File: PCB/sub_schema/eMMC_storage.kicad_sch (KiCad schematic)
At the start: 26 parts, among them U10 MTFC32GAZAQHD-WT, U8 MTFC32GAZAQHD-WT

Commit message: worked on BOM
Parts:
- C29, C30, C31, C32, C35, C36, C37, C38, C39, C40, C42, C43, C44, C45, C46, C48, C49, C50, C51, C52: footprint (none) -> Capacitor_SMD:C_0201_0603Metric
- C33, C34, C41, C47: footprint (none) -> Capacitor_SMD:C_0402_1005Metric
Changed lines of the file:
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@@
 			)
 		)
-		(property "Footprint" ""
+		(property "Footprint" "Capacitor_SMD:C_0201_0603Metric"
 			(at 88.9 27.94 0)
 			(effects
@@
 			)
 		)
-		(property "Footprint" ""
+		(property "Footprint" "Capacitor_SMD:C_0201_0603Metric"
 			(at 124.46 27.94 0)
 			(effects
@@
 			)
 		)
-		(property "Footprint" ""
+		(property "Footprint" "Capacitor_SMD:C_0201_0603Metric"
 			(at 31.75 128.27 0)
 			(effects
@@
 			)
 		)
-		(property "Footprint" ""
+		(property "Footprint" "Capacitor_SMD:C_0201_0603Metric"
 			(at 36.83 29.21 0)
 			(effects
@@
 			)
 		)
-		(property "Footprint" ""
+		(property "Footprint" "Capacitor_SMD:C_0201_0603Metric"
 			(at 54.61 29.21 0)
 			(effects
@@
 			)
 		)
-		(property "Footprint" ""
+		(property "Footprint" "Capacitor_SMD:C_0201_0603Metric"
 			(at 106.68 27.94 0)
 			(effects
@@
 			)
 		)
-		(property "Footprint" ""
+		(property "Footprint" "Capacitor_SMD:C_0201_0603Metric"
 			(at 270.51 29.21 0)
 			(effects
@@
 			)
 		)
-		(property "Footprint" ""
+		(property "Footprint" "Capacitor_SMD:C_0201_0603Metric"
 			(at 261.62 29.21 0)
 			(effects
@@
 			)
 		)
-		(property "Footprint" ""
+		(property "Footprint" "Capacitor_SMD:C_0201_0603Metric"
 			(at 97.79 27.94 0)
 			(effects
@@
 			)
 		)
-		(property "Footprint" ""
+		(property "Footprint" "Capacitor_SMD:C_0201_0603Metric"
 			(at 252.73 29.21 0)
 			(effects
@@
 			)
 		)
-		(property "Footprint" ""
+		(property "Footprint" "Capacitor_SMD:C_0201_0603Metric"
 			(at 182.88 30.48 0)
 			(effects
@@
 			)
 		)
-		(property "Footprint" ""
+		(property "Footprint" "Capacitor_SMD:C_0402_1005Metric"
 			(at 29.21 29.21 0)
 			(effects
@@
 			)
 		)
-		(property "Footprint" ""
+		(property "Footprint" "Capacitor_SMD:C_0201_0603Metric"
 			(at 45.72 29.21 0)
 			(effects
@@
 			)
 		)
-		(property "Footprint" ""
+		(property "Footprint" "Capacitor_SMD:C_0201_0603Metric"
 			(at 200.66 30.48 0)
 			(effects
@@
 			)
 		)
-		(property "Footprint" ""
+		(property "Footprint" "Capacitor_SMD:C_0402_1005Metric"
 			(at 81.28 27.94 0)
 			(effects
@@
 			)
 		)
-		(property "Footprint" ""
+		(property "Footprint" "Capacitor_SMD:C_0201_0603Metric"
 			(at 165.1 129.54 0)
 			(effects
@@
 			)
 		)
-		(property "Footprint" ""
+		(property "Footprint" "Capacitor_SMD:C_0201_0603Metric"
 			(at 115.57 27.94 0)
 			(effects
@@
 			)
 		)
-		(property "Footprint" ""
+		(property "Footprint" "Capacitor_SMD:C_0402_1005Metric"
 			(at 175.26 30.48 0)
 			(effects
@@
 			)
 		)
-		(property "Footprint" ""
+		(property "Footprint" "Capacitor_SMD:C_0201_0603Metric"
 			(at 63.5 29.21 0)
 			(effects
@@
 			)
 		)
-		(property "Footprint" ""
+		(property "Footprint" "Capacitor_SMD:C_0201_0603Metric"
 			(at 243.84 29.21 0)
 			(effects
@@
 			)
 		)
-		(property "Footprint" ""
+		(property "Footprint" "Capacitor_SMD:C_0201_0603Metric"
 			(at 191.77 30.48 0)
 			(effects
@@
 			)
 		)
-		(property "Footprint" ""
+		(property "Footprint" "Capacitor_SMD:C_0201_0603Metric"
 			(at 234.95 29.21 0)
 			(effects
@@
 			)
 		)
-		(property "Footprint" ""
+		(property "Footprint" "Capacitor_SMD:C_0402_1005Metric"
 			(at 227.33 29.21 0)
 			(effects
@@
 			)
 		)
-		(property "Footprint" ""
+		(property "Footprint" "Capacitor_SMD:C_0201_0603Metric"
 			(at 209.55 30.48 0)
 			(effects

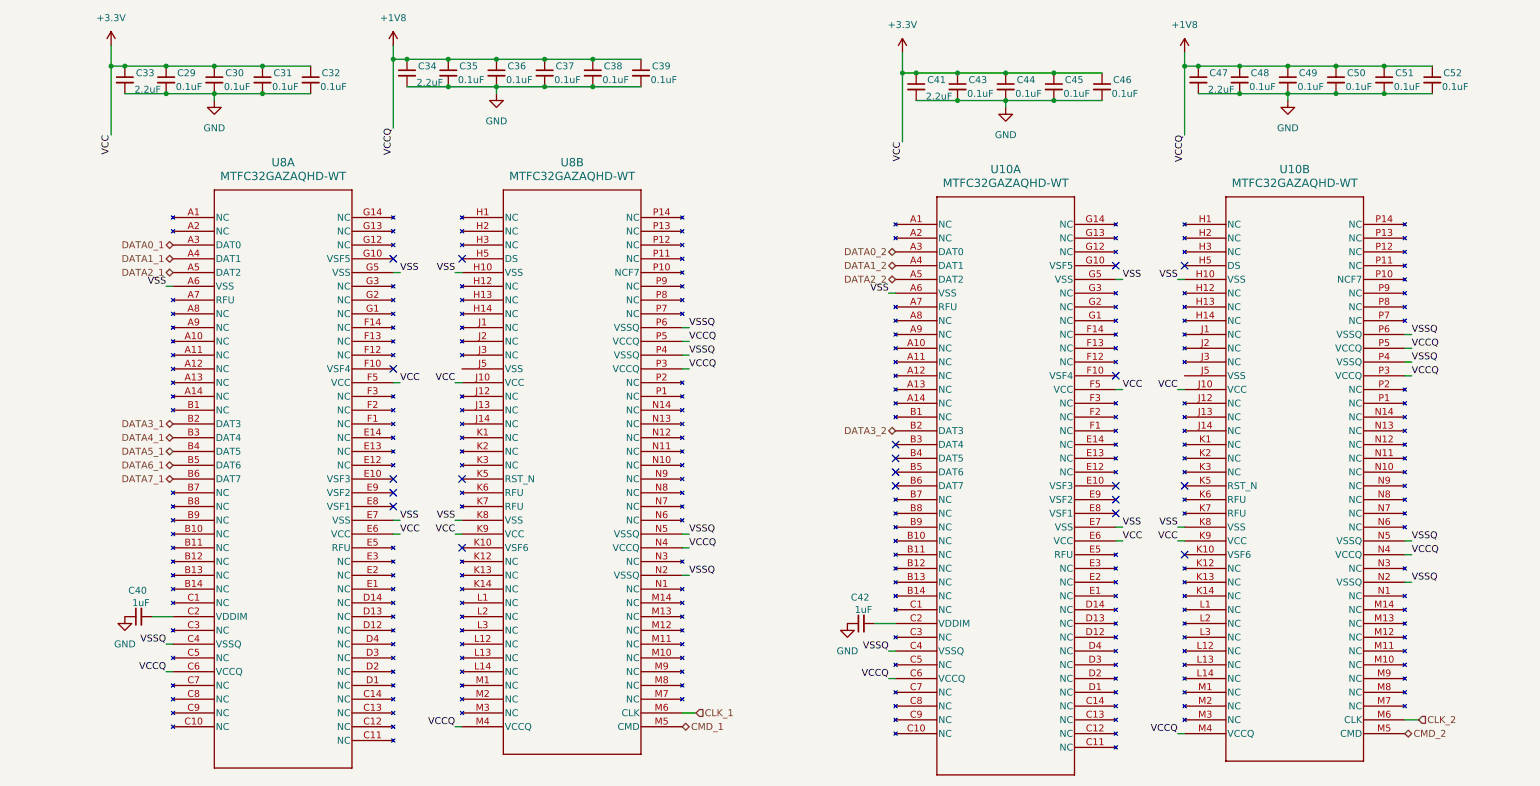
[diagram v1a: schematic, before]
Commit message: added footprints and BOM
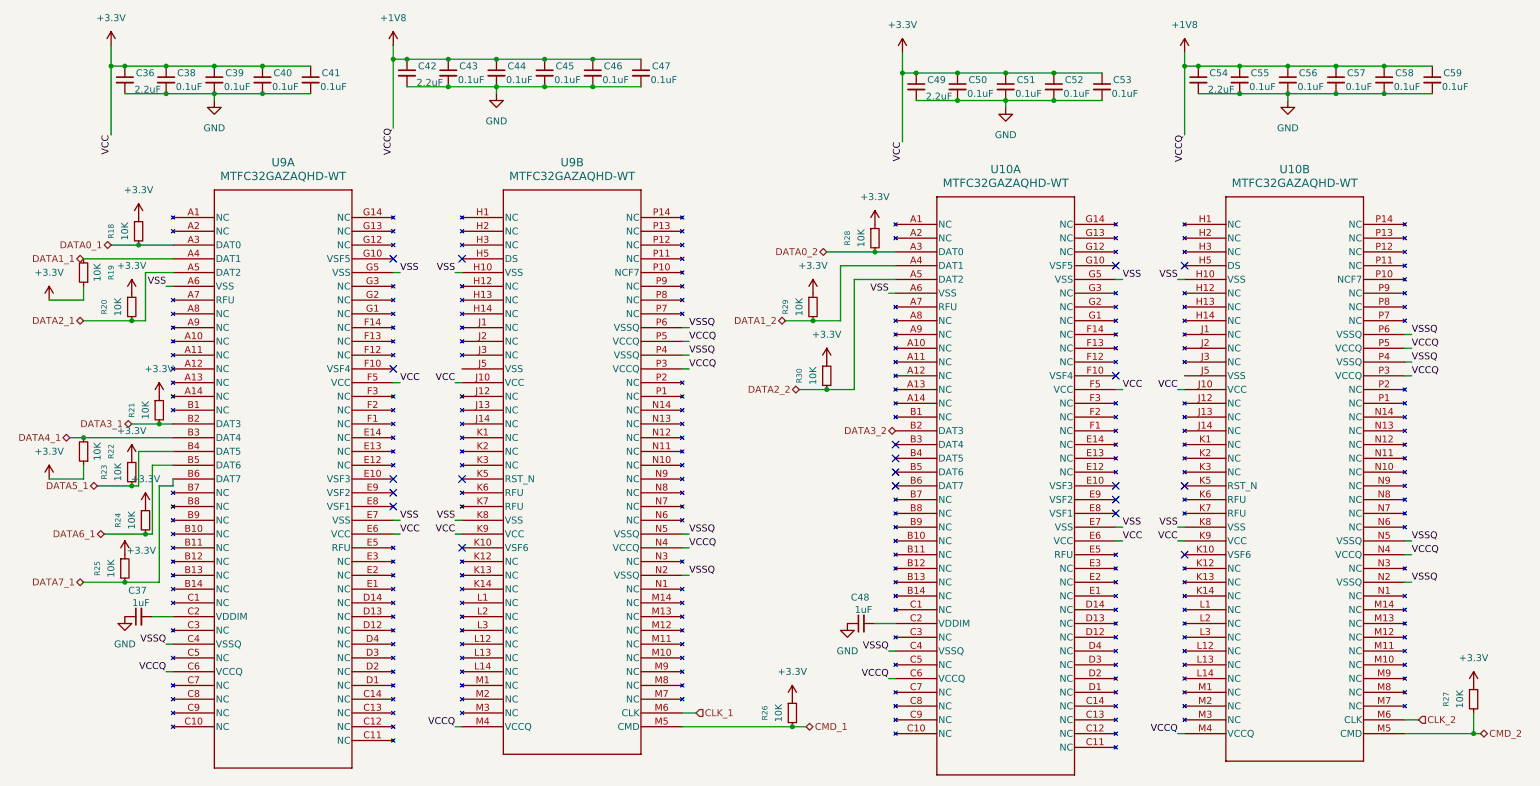
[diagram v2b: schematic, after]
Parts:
- added R18, R19, R20, R21, R22, R23, R24, R25, R26, R27, R28, R29, R30: 10K, Resistor_SMD:R_0201_0603Metric, symbol Device:R_Small
- U10: footprint (none) -> Package_BGA:LFBGA-153_11.5x13mm_Layout14x14_P0.5mm
- U9: renamed from U8; footprint (none) -> Package_BGA:LFBGA-153_11.5x13mm_Layout14x14_P0.5mm
- renumbered C33 to C36, C40 to C37, C29 to C38, C30 to C39, C31 to C40, C32 to C41, C34 to C42, C35 to C43, C36 to C44, C37 to C45, C38 to C46, C39 to C47, C42 to C48, C41 to C49, C43 to C50, C44 to C51, C45 to C52, C46 to C53, C47 to C54, C48 to C55, C49 to C56, C50 to C57, C51 to C58, C52 to C59
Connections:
- net +3.3V: now also R18.1, R19.1, R20.1, R21.1, R22.1, R23.1, R24.1, R25.1, R26.1, R27.1, R28.1, R29.1, R30.1
- net CMD_1: now also R26.2
- net CMD_2: now also R27.2
- net DATA0_1: now also R18.2
- net DATA0_2: now also R28.2
- net DATA1_1: now also R19.2
- net DATA1_2: now also R29.2
- net DATA2_1: now also R20.2
- net DATA2_2: now also R30.2
- net DATA3_1: now also R21.2
- net DATA4_1: now also R22.2
- net DATA5_1: now also R23.2
- net DATA6_1: now also R24.2
- net DATA7_1: now also R25.2
